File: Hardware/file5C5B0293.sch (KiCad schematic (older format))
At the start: 19 parts, among them J15 Conn_01x06_Male, J16 Conn_ARM_JTAG_SWD_10, U12 STM32F030R8Tx

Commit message: Updated schematic
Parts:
- renumbered C49 to C54, C50 to C55, C51 to C56, C52 to C57, C53 to C58, C54 to C59, C55 to C60, C56 to C61, C57 to C62, C58 to C63, C59 to C64, C60 to C65, C61 to C66, C62 to C67, C63 to C68, C64 to C69, J15 to J16, J16 to J17, U12 to U13
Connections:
- net MODE_SW: now also U13.41 (PA8); no longer U13.24 (PC4)
- net SET_SW: now reaches U13.44 (PA11)
- new net SET_CV: U13.24 (PC4)
- no-connect marks 20 -> 18
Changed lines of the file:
@@
 $EndDescr
 $Comp
-L MCU_ST_STM32F0:STM32F030R8Tx U12
+L MCU_ST_STM32F0:STM32F030R8Tx U13
 U 1 1 5BDDCB3B
 P 6350 3550
-F 0 "U12" H 6350 1664 50  0000 C CNN
+F 0 "U13" H 6350 1664 50  0000 C CNN
 F 1 "STM32F030R8Tx" H 6350 1573 50  0000 C CNN
 F 2 "Package_QFP:LQFP-64_10x10mm_P0.5mm" H 5850 1850 50  0001 R CNN
@@
 $EndComp
 $Comp
-L power:+3.3V #PWR0220
+L power:+3.3V #PWR0135
 U 1 1 5C3E306A
 P 1450 7000
-F 0 "#PWR0220" H 1450 6850 50  0001 C CNN
+F 0 "#PWR0135" H 1450 6850 50  0001 C CNN
 F 1 "+3.3V" H 1465 7173 50  0000 C CNN
 F 2 "" H 1450 7000 50  0001 C CNN
@@
 	1450 7000 1450 7050
 $Comp
-L power:GND #PWR0221
+L power:GND #PWR0136
 U 1 1 5C3E8151
 P 1450 7550
-F 0 "#PWR0221" H 1450 7300 50  0001 C CNN
+F 0 "#PWR0136" H 1450 7300 50  0001 C CNN
 F 1 "GND" H 1455 7377 50  0000 C CNN
 F 2 "" H 1450 7550 50  0001 C CNN
@@
 $EndComp
 $Comp
-L power:+3.3V #PWR0222
+L power:+3.3V #PWR0146
 U 1 1 5C3F5FB1
 P 6350 1550
-F 0 "#PWR0222" H 6350 1400 50  0001 C CNN
+F 0 "#PWR0146" H 6350 1400 50  0001 C CNN
 F 1 "+3.3V" H 6365 1723 50  0000 C CNN
 F 2 "" H 6350 1550 50  0001 C CNN
@@
 	6350 1650 6250 1650
 $Comp
-L power:GND #PWR0223
+L power:GND #PWR0147
 U 1 1 5C3FCAA5
 P 6350 5650
-F 0 "#PWR0223" H 6350 5400 50  0001 C CNN
+F 0 "#PWR0147" H 6350 5400 50  0001 C CNN
 F 1 "GND" H 6355 5477 50  0000 C CNN
 F 2 "" H 6350 5650 50  0001 C CNN
@@
 Wire Wire Line
 	7100 2650 6950 2650
-Text GLabel 5600 4050 0    50   Input ~ 0
+Text GLabel 7100 2750 2    50   Input ~ 0
 MODE_SW
 Wire Wire Line
@@
 	6350 1550 6350 1650
 $Comp
-L power:+3.3VA #PWR021
+L power:+3.3VA #PWR0148
 U 1 1 5BEED548
 P 6650 1550
-F 0 "#PWR021" H 6650 1400 50  0001 C CNN
+F 0 "#PWR0148" H 6650 1400 50  0001 C CNN
 F 1 "+3.3VA" H 6665 1723 50  0000 C CNN
 F 2 "" H 6650 1550 50  0001 C CNN
@@
 	6550 1650 6550 1750
 $Comp
-L Device:C C56
+L Device:C C61
 U 1 1 5BEF0667
 P 3250 6000
-F 0 "C56" H 3365 6046 50  0000 L CNN
+F 0 "C61" H 3365 6046 50  0000 L CNN
 F 1 "100 nF" H 3365 5955 50  0000 L CNN
 F 2 "Capacitor_SMD:C_0603_1608Metric" H 3288 5850 50  0001 C CNN
@@
 $EndComp
 $Comp
-L Device:C C54
+L Device:C C59
 U 1 1 5BEF066E
 P 2750 6000
-F 0 "C54" H 2865 6046 50  0000 L CNN
+F 0 "C59" H 2865 6046 50  0000 L CNN
 F 1 "10 nF" H 2865 5955 50  0000 L CNN
 F 2 "Capacitor_SMD:C_0603_1608Metric" H 2788 5850 50  0001 C CNN
@@
 $EndComp
 $Comp
-L Device:C C58
+L Device:C C63
 U 1 1 5BEF067C
 P 3750 6000
-F 0 "C58" H 3865 6046 50  0000 L CNN
+F 0 "C63" H 3865 6046 50  0000 L CNN
 F 1 "1 uF" H 3865 5955 50  0000 L CNN
 F 2 "Capacitor_Tantalum_SMD:CP_EIA-2012-12_Kemet-R" H 3788 5850 50  0001 C CNN
@@
 $EndComp
 $Comp
-L Device:CP C59
+L Device:CP C64
 U 1 1 5BEF0698
 P 4250 6000
-F 0 "C59" H 4368 6046 50  0000 L CNN
+F 0 "C64" H 4368 6046 50  0000 L CNN
 F 1 "10 uF" H 4368 5955 50  0000 L CNN
 F 2 "Capacitor_SMD:CP_Elec_4x5.7" H 4288 5850 50  0001 C CNN
@@
 	2750 5700 2750 5850
 $Comp
-L power:GND #PWR015
+L power:GND #PWR0140
 U 1 1 5BEF06E1
 P 3450 6250
-F 0 "#PWR015" H 3450 6000 50  0001 C CNN
+F 0 "#PWR0140" H 3450 6000 50  0001 C CNN
 F 1 "GND" H 3455 6077 50  0000 C CNN
 F 2 "" H 3450 6250 50  0001 C CNN
@@
 	2750 6150 2750 6250
 $Comp
-L power:+3.3VA #PWR016
+L power:+3.3VA #PWR0141
 U 1 1 5BEF77DE
 P 3500 5650
-F 0 "#PWR016" H 3500 5500 50  0001 C CNN
+F 0 "#PWR0141" H 3500 5500 50  0001 C CNN
 F 1 "+3.3VA" H 3515 5823 50  0000 C CNN
 F 2 "" H 3500 5650 50  0001 C CNN
@@
 	3500 5650 3500 5700
 $Comp
-L power:GND #PWR012
+L power:GND #PWR0137
 U 1 1 5BF2206A
 P 1900 3050
-F 0 "#PWR012" H 1900 2800 50  0001 C CNN
+F 0 "#PWR0137" H 1900 2800 50  0001 C CNN
 F 1 "GND" H 1905 2877 50  0000 C CNN
 F 2 "" H 1900 3050 50  0001 C CNN
@@
 	3750 6250 4250 6250
 $Comp
-L Device:C C49
+L Device:C C54
 U 1 1 5BF63F9B
 P 650 7250
-F 0 "C49" H 765 7296 50  0000 L CNN
+F 0 "C54" H 765 7296 50  0000 L CNN
 F 1 "100 nF" H 765 7205 50  0000 L CNN
 F 2 "Capacitor_SMD:C_0603_1608Metric" H 688 7100 50  0001 C CNN
@@
 $EndComp
 $Comp
-L Device:C C50
+L Device:C C55
 U 1 1 5BF640D3
 P 1150 7250
-F 0 "C50" H 1265 7296 50  0000 L CNN
+F 0 "C55" H 1265 7296 50  0000 L CNN
 F 1 "100 nF" H 1265 7205 50  0000 L CNN
 F 2 "Capacitor_SMD:C_0603_1608Metric" H 1188 7100 50  0001 C CNN
@@
 $EndComp
 $Comp
-L Device:C C51
+L Device:C C56
 U 1 1 5BF64109
 P 1650 7250
-F 0 "C51" H 1765 7296 50  0000 L CNN
+F 0 "C56" H 1765 7296 50  0000 L CNN
 F 1 "100 nF" H 1765 7205 50  0000 L CNN
 F 2 "Capacitor_SMD:C_0603_1608Metric" H 1688 7100 50  0001 C CNN
@@
 $EndComp
 $Comp
-L Device:CP C52
+L Device:CP C57
 U 1 1 5BF64143
 P 2200 7250
-F 0 "C52" H 2318 7296 50  0000 L CNN
+F 0 "C57" H 2318 7296 50  0000 L CNN
 F 1 "4.7 uF" H 2318 7205 50  0000 L CNN
 F 2 "Capacitor_Tantalum_SMD:CP_EIA-3216-18_Kemet-A" H 2238 7100 50  0001 C CNN
@@
 	1150 7450 1450 7450
 $Comp
-L power:+3.3V #PWR017
+L power:+3.3V #PWR0142
 U 1 1 5BF7E841
 P 3500 7000
-F 0 "#PWR017" H 3500 6850 50  0001 C CNN
+F 0 "#PWR0142" H 3500 6850 50  0001 C CNN
 F 1 "+3.3V" H 3515 7173 50  0000 C CNN
 F 2 "" H 3500 7000 50  0001 C CNN
@@
 	3500 7000 3500 7050
 $Comp
-L power:GND #PWR018
+L power:GND #PWR0143
 U 1 1 5BF7E848
 P 3500 7550
-F 0 "#PWR018" H 3500 7300 50  0001 C CNN
+F 0 "#PWR0143" H 3500 7300 50  0001 C CNN
 F 1 "GND" H 3505 7377 50  0000 C CNN
 F 2 "" H 3500 7550 50  0001 C CNN
@@
 $EndComp
 $Comp
-L Device:C C53
+L Device:C C58
 U 1 1 5BF7E84E
 P 2700 7250
-F 0 "C53" H 2815 7296 50  0000 L CNN
+F 0 "C58" H 2815 7296 50  0000 L CNN
 F 1 "100 nF" H 2815 7205 50  0000 L CNN
 F 2 "Capacitor_SMD:C_0603_1608Metric" H 2738 7100 50  0001 C CNN
@@
 $EndComp
 $Comp
-L Device:C C55
+L Device:C C60
 U 1 1 5BF7E855
 P 3200 7250
-F 0 "C55" H 3315 7296 50  0000 L CNN
+F 0 "C60" H 3315 7296 50  0000 L CNN
 F 1 "100 nF" H 3315 7205 50  0000 L CNN
 F 2 "Capacitor_SMD:C_0603_1608Metric" H 3238 7100 50  0001 C CNN
@@
 $EndComp
 $Comp
-L Device:C C57
+L Device:C C62
 U 1 1 5BF7E85C
 P 3700 7250
-F 0 "C57" H 3815 7296 50  0000 L CNN
+F 0 "C62" H 3815 7296 50  0000 L CNN
 F 1 "100 nF" H 3815 7205 50  0000 L CNN
 F 2 "Capacitor_SMD:C_0603_1608Metric" H 3738 7100 50  0001 C CNN
@@
 $EndComp
 $Comp
-L Device:CP C60
+L Device:CP C65
 U 1 1 5BF7E863
 P 4250 7250
-F 0 "C60" H 4368 7296 50  0000 L CNN
+F 0 "C65" H 4368 7296 50  0000 L CNN
 F 1 "4.7 uF" H 4368 7205 50  0000 L CNN
 F 2 "Capacitor_Tantalum_SMD:CP_EIA-3216-18_Kemet-A" H 4288 7100 50  0001 C CNN
@@
 	3200 7450 3500 7450
 $Comp
-L power:+3.3V #PWR019
+L power:+3.3V #PWR0144
 U 1 1 5BF821BD
 P 5550 7000
-F 0 "#PWR019" H 5550 6850 50  0001 C CNN
+F 0 "#PWR0144" H 5550 6850 50  0001 C CNN
 F 1 "+3.3V" H 5565 7173 50  0000 C CNN
 F 2 "" H 5550 7000 50  0001 C CNN
@@
 	5550 7000 5550 7050
 $Comp
-L power:GND #PWR020
+L power:GND #PWR0145
 U 1 1 5BF821C4
 P 5550 7550
-F 0 "#PWR020" H 5550 7300 50  0001 C CNN
+F 0 "#PWR0145" H 5550 7300 50  0001 C CNN
 F 1 "GND" H 5555 7377 50  0000 C CNN
 F 2 "" H 5550 7550 50  0001 C CNN
@@
 $EndComp
 $Comp
-L Device:C C61
+L Device:C C66
 U 1 1 5BF821CA
 P 4750 7250
-F 0 "C61" H 4865 7296 50  0000 L CNN
+F 0 "C66" H 4865 7296 50  0000 L CNN
 F 1 "100 nF" H 4865 7205 50  0000 L CNN
 F 2 "Capacitor_SMD:C_0603_1608Metric" H 4788 7100 50  0001 C CNN
@@
 $EndComp
 $Comp
-L Device:C C62
+L Device:C C67
 U 1 1 5BF821D1
 P 5250 7250
-F 0 "C62" H 5365 7296 50  0000 L CNN
+F 0 "C67" H 5365 7296 50  0000 L CNN
 F 1 "100 nF" H 5365 7205 50  0000 L CNN
 F 2 "Capacitor_SMD:C_0603_1608Metric" H 5288 7100 50  0001 C CNN
@@
 $EndComp
 $Comp
-L Device:C C63
+L Device:C C68
 U 1 1 5BF821D8
 P 5750 7250
-F 0 "C63" H 5865 7296 50  0000 L CNN
+F 0 "C68" H 5865 7296 50  0000 L CNN
 F 1 "100 nF" H 5865 7205 50  0000 L CNN
 F 2 "Capacitor_SMD:C_0603_1608Metric" H 5788 7100 50  0001 C CNN
@@
 $EndComp
 $Comp
-L Device:CP C64
+L Device:CP C69
 U 1 1 5BF821DF
 P 6300 7250
-F 0 "C64" H 6418 7296 50  0000 L CNN
+F 0 "C69" H 6418 7296 50  0000 L CNN
 F 1 "4.7 uF" H 6418 7205 50  0000 L CNN
 F 2 "Capacitor_Tantalum_SMD:CP_EIA-3216-18_Kemet-A" H 6338 7100 50  0001 C CNN
@@
 	5250 7450 5550 7450
 $Comp
-L Connector:Conn_ARM_JTAG_SWD_10 J16
+L Connector:Conn_ARM_JTAG_SWD_10 J17
 U 1 1 5BF86C4D
 P 1950 2250
-F 0 "J16" H 1510 2296 50  0000 R CNN
+F 0 "J17" H 1510 2296 50  0000 R CNN
 F 1 "Conn_ARM_JTAG_SWD_10" H 1510 2205 50  0000 R CNN
 F 2 "Connector_PinHeader_2.54mm:PinHeader_2x05_P2.54mm_Vertical" H 2000 1700 50  0001 L TNN
@@
 Connection ~ 1900 2950
 $Comp
-L power:+3.3V #PWR013
+L power:+3.3V #PWR0138
 U 1 1 5BF90955
 P 1950 1600
-F 0 "#PWR013" H 1950 1450 50  0001 C CNN
+F 0 "#PWR0138" H 1950 1450 50  0001 C CNN
 F 1 "+3.3V" H 1965 1773 50  0000 C CNN
 F 2 "" H 1950 1600 50  0001 C CNN
@@
 	2600 2150 2450 2150
 $Comp
-L Connector:Conn_01x06_Male J15
+L Connector:Conn_01x06_Male J16
 U 1 1 5BFB55EB
 P 1850 3800
-F 0 "J15" H 1822 3680 50  0000 R CNN
+F 0 "J16" H 1822 3680 50  0000 R CNN
 F 1 "Conn_01x06_Male" H 1822 3771 50  0000 R CNN
 F 2 "Connector_PinHeader_2.54mm:PinHeader_1x06_P2.54mm_Vertical" H 1850 3800 50  0001 C CNN
@@
 	2200 3700 2050 3700
 $Comp
-L power:GND #PWR014
+L power:GND #PWR0139
 U 1 1 5BFD1A9D
 P 2200 4050
-F 0 "#PWR014" H 2200 3800 50  0001 C CNN
+F 0 "#PWR0139" H 2200 3800 50  0001 C CNN
 F 1 "GND" H 2205 3877 50  0000 C CNN
 F 2 "" H 2200 4050 50  0001 C CNN
@@
 NoConn ~ 5750 3250
 NoConn ~ 5750 3150
-NoConn ~ 6950 2750
-NoConn ~ 6950 3050
 NoConn ~ 6950 3150
 NoConn ~ 2450 2350
 NoConn ~ 2450 2450
+Wire Wire Line
+	7100 2750 6950 2750
+Text GLabel 5600 4050 0    50   Input ~ 0
+SET_CV
+Text GLabel 7100 3050 2    50   Input ~ 0
+SET_SW
+Wire Wire Line
+	7100 3050 6950 3050
 $EndSCHEMATC

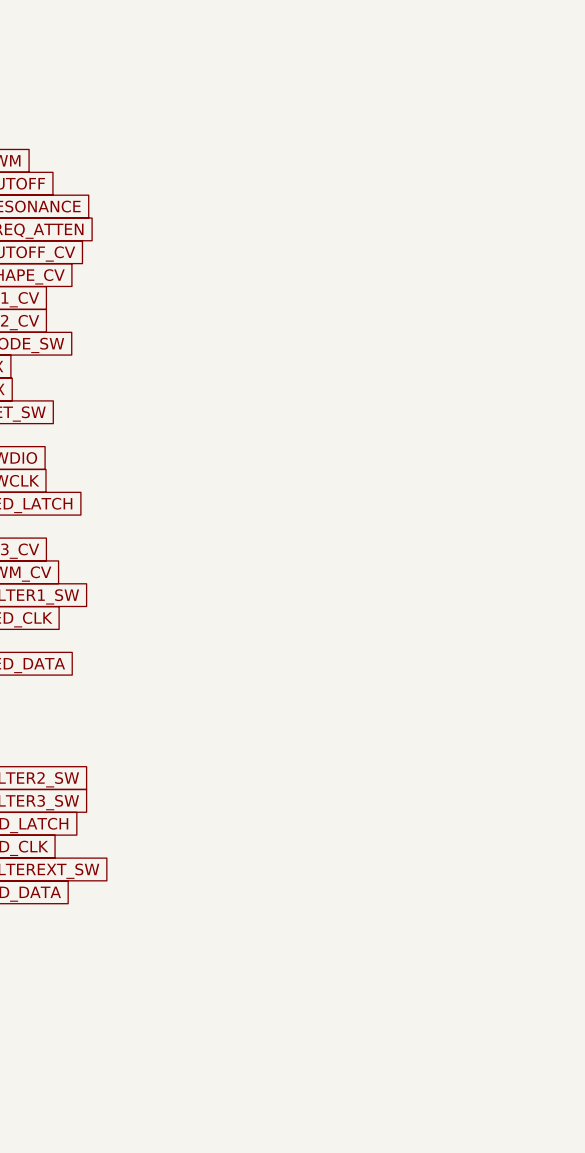
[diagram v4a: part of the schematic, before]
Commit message: Added new MCU
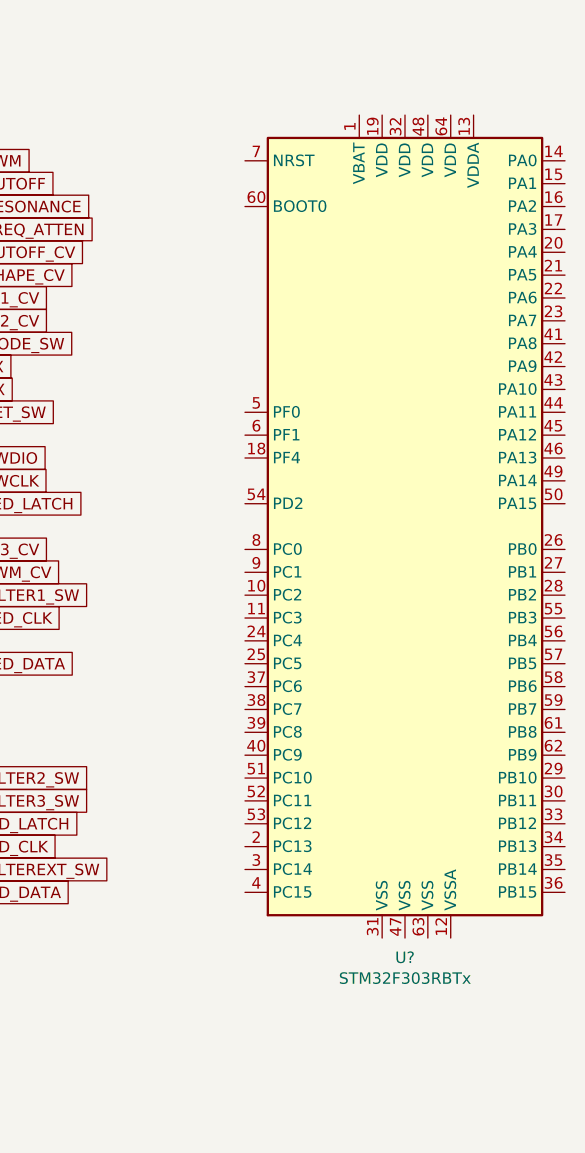
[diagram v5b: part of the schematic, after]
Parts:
- added U?: STM32F303RBTx, Package_QFP:LQFP-64_10x10mm_P0.5mm, symbol MCU_ST_STM32F3:STM32F303RBTx
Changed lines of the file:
@@
 Wire Wire Line
 	7100 3050 6950 3050
+$Comp
+L MCU_ST_STM32F3:STM32F303RBTx U?
+U 1 1 5BDFE304
+P 9000 3550
+F 0 "U?" H 9000 1664 50  0000 C CNN
+F 1 "STM32F303RBTx" H 9000 1573 50  0000 C CNN
+F 2 "Package_QFP:LQFP-64_10x10mm_P0.5mm" H 8400 1850 50  0001 R CNN
+F 3 "http://www.st.com/st-web-ui/static/active/en/resource/technical/document/datasheet/DM00058181.pdf" H 9000 3550 50  0001 C CNN
+	1    9000 3550
+	1    0    0    -1
+$EndComp
 $EndSCHEMATC

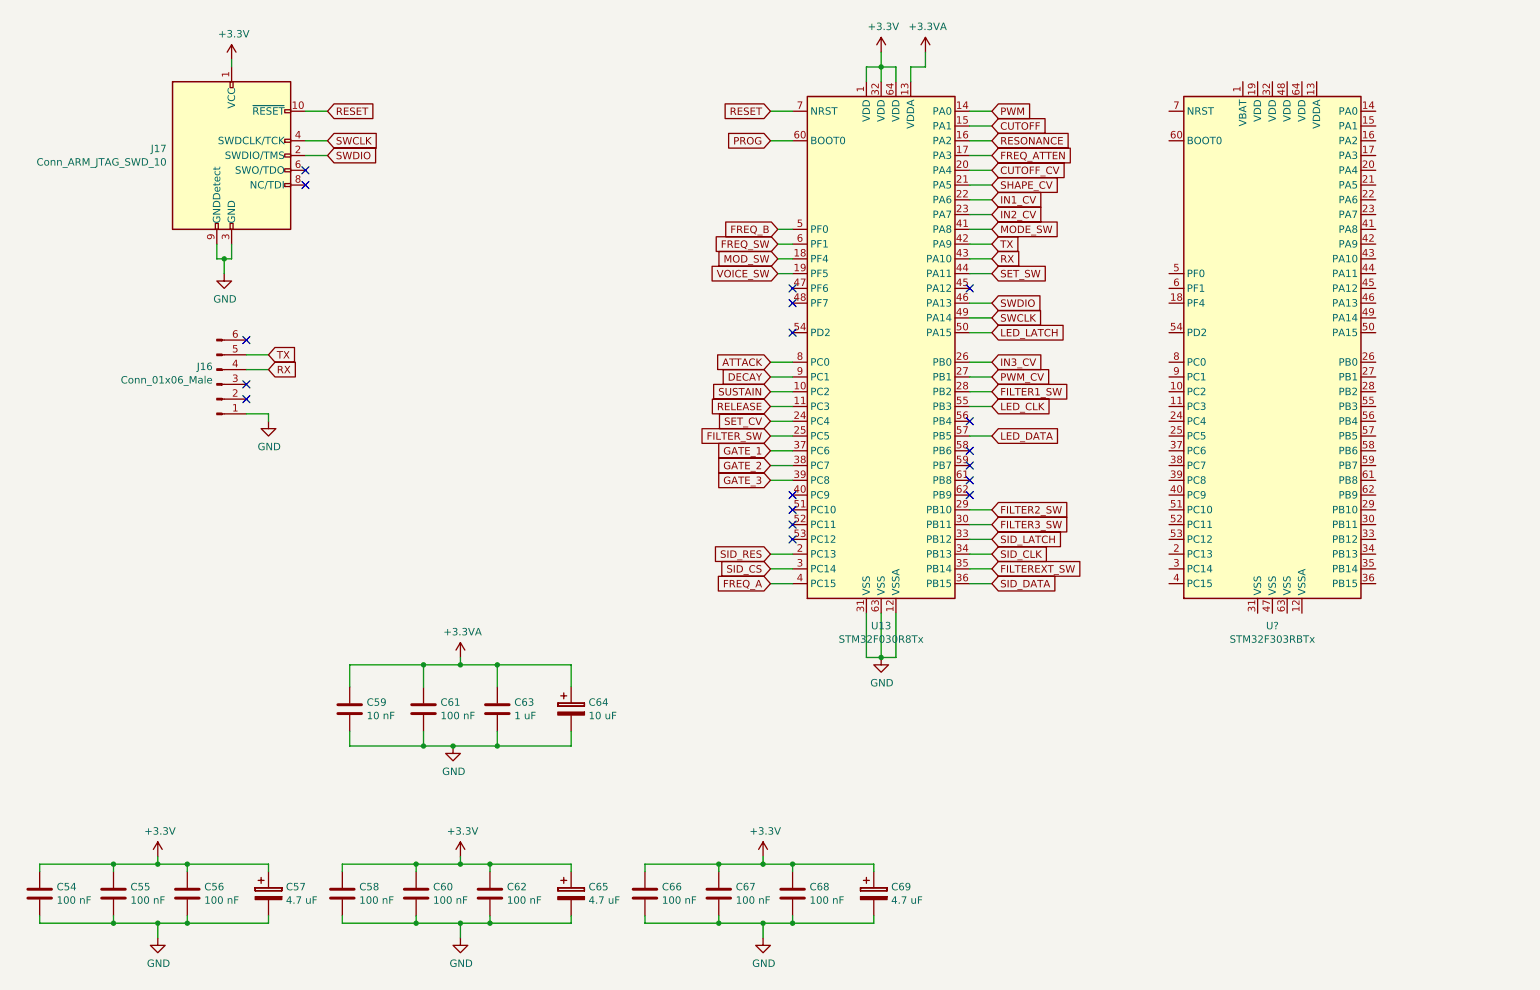
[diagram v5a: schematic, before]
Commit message: Finished updating MCU pinouts
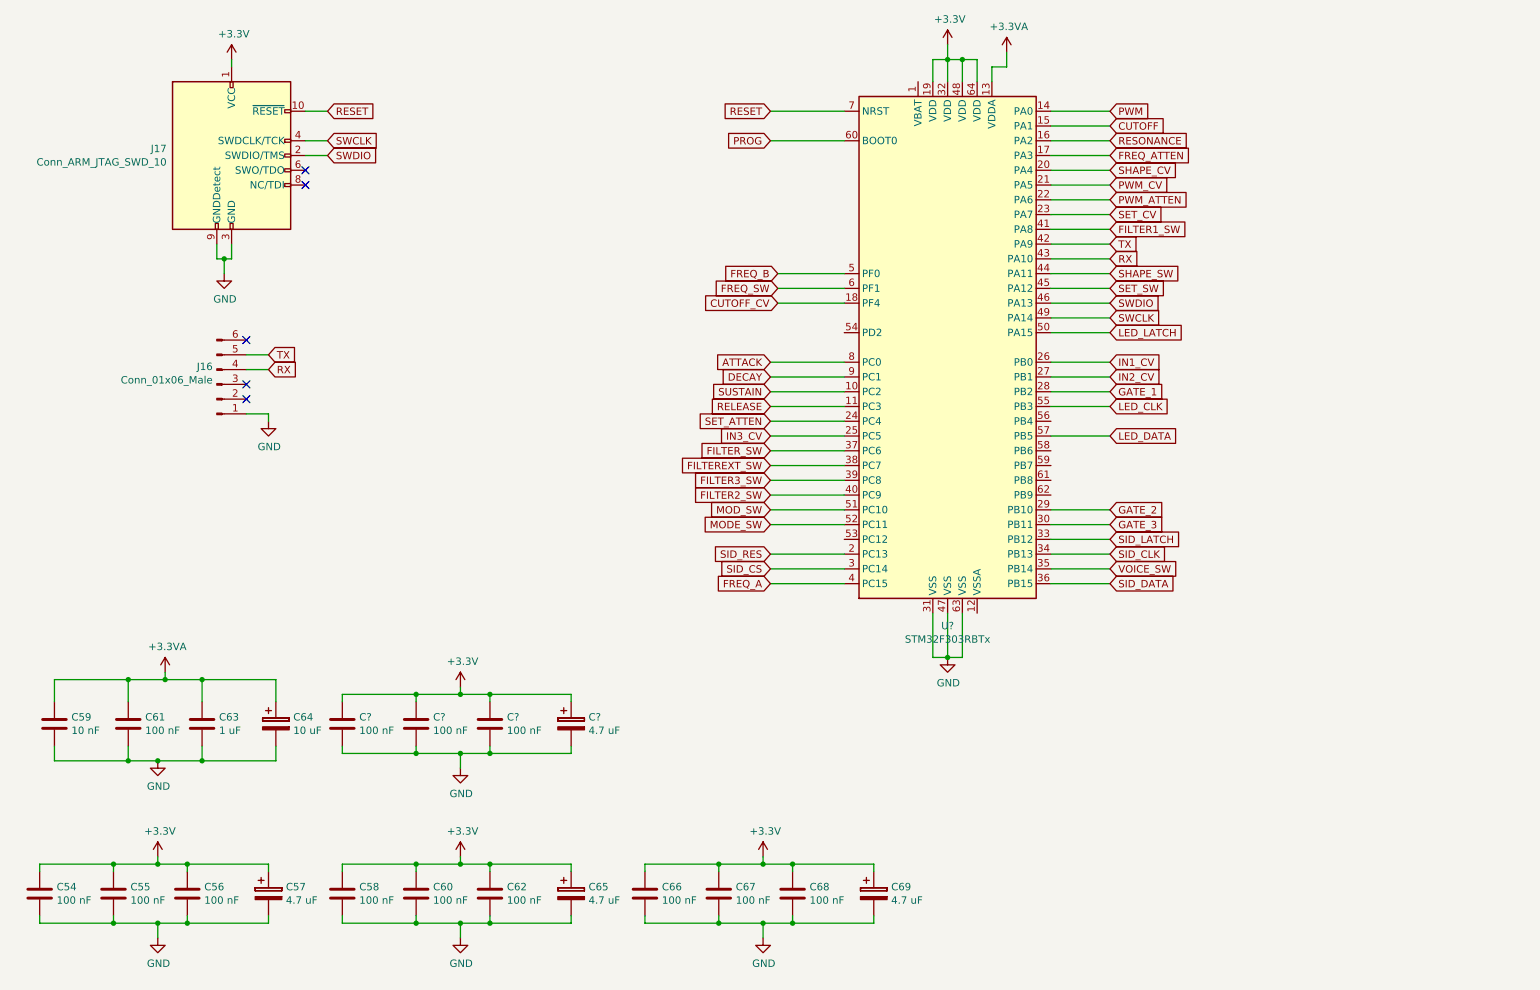
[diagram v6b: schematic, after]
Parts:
- removed U13: STM32F030R8Tx, Package_QFP:LQFP-64_10x10mm_P0.5mm, symbol MCU_ST_STM32F0:STM32F030R8Tx
- added C? (x3): 100 nF, Capacitor_SMD:C_0603_1608Metric, symbol Device:C
- added C?: 4.7 uF, Capacitor_Tantalum_SMD:CP_EIA-3216-18_Kemet-A, symbol Device:CP
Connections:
- net +3.3VA: now also U?.13 (VDDA)
- net +3V3: now also U?.19 (VDD), U?.32 (VDD), U?.48 (VDD), U?.64 (VDD), C?.1, C?.1, C?.1, C?.1
- net ATTACK: now also U?.8 (PC0)
- net CUTOFF: now also U?.15 (PA1)
- net CUTOFF_CV: now also U?.18 (PF4)
- net DECAY: now also U?.9 (PC1)
- net FILTER1_SW: now also U?.41 (PA8)
- net FILTER2_SW: now also U?.40 (PC9)
- net FILTER3_SW: now also U?.39 (PC8)
- net FILTEREXT_SW: now also U?.38 (PC7)
- net FILTER_SW: now also U?.37 (PC6)
- net FREQ_A: now also U?.4 (PC15)
- net FREQ_ATTEN: now also U?.17 (PA3)
- net FREQ_B: now also U?.5 (PF0)
- net FREQ_SW: now also U?.6 (PF1)
- net GATE_1: now also U?.28 (PB2)
- net GATE_2: now also U?.29 (PB10)
- net GATE_3: now also U?.30 (PB11)
- net GND: now also U?.31 (VSS), U?.47 (VSS), U?.63 (VSS), C?.2, C?.2, C?.2, C?.2
- net IN1_CV: now also U?.26 (PB0)
- net IN2_CV: now also U?.27 (PB1)
- net IN3_CV: now also U?.25 (PC5)
- net LED_CLK: now also U?.55 (PB3)
- net LED_DATA: now also U?.57 (PB5)
- net LED_LATCH: now also U?.50 (PA15)
- net MODE_SW: now also U?.52 (PC11)
- net MOD_SW: now also U?.51 (PC10)
- net PROG: now also U?.60 (BOOT0)
- net PWM: now also U?.14 (PA0)
- net PWM_CV: now also U?.21 (PA5)
- net RELEASE: now also U?.11 (PC3)
- net RESET: now also U?.7 (NRST)
- net RESONANCE: now also U?.16 (PA2)
- net RX: now also U?.43 (PA10)
- net SET_CV: now also U?.23 (PA7)
- net SET_SW: now also U?.45 (PA12)
- net SHAPE_CV: now also U?.20 (PA4)
- net SID_CLK: now also U?.34 (PB13)
- net SID_CS: now also U?.3 (PC14)
- net SID_DATA: now also U?.36 (PB15)
- net SID_LATCH: now also U?.33 (PB12)
- net SID_RES: now also U?.2 (PC13)
- net SUSTAIN: now also U?.10 (PC2)
- net SWCLK: now also U?.49 (PA14)
- net SWDIO: now also U?.46 (PA13)
- net TX: now also U?.42 (PA9)
- net VOICE_SW: now also U?.35 (PB14)
- net PWM_ATTEN: now reaches U?.22 (PA6)
- net SET_ATTEN: now reaches U?.24 (PC4)
- net SHAPE_SW: now reaches U?.44 (PA11)
- no-connect marks 18 -> 5
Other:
- moved on the sheet: C59, C61, C63, C64, U?
